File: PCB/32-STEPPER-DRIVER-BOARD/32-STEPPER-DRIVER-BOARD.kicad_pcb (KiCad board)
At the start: 4 copper layers, 100 x 100 mm, 346 parts, among them J1 MEC2-30-01-X-TH1-NP-WT, J2 MEC2-30-01-X-TH1-NP-WT, J3 MEC2-30-01-X-TH1-NP-WT, J4 MEC2-30-01-X-TH1-NP-WT, J5 IPS1-125-01-S-D, J6 UMPT-06-01-X-RA-WT-P-X, U1 74HC595, U10 74HC595, U11 74HC595, U12 74HC595, U13 74HC595, U14 74HC595, U15 74HC595, U17 74HC595, U18 74HC595, U19 74HC595, U2 74HC595, U20 74HC595, U21 74HC595, U22 74HC595, U3 74HC595, U4 74HC595, U5 74HC595, U6 74HC595, U7 74HC595, U9 74HC595

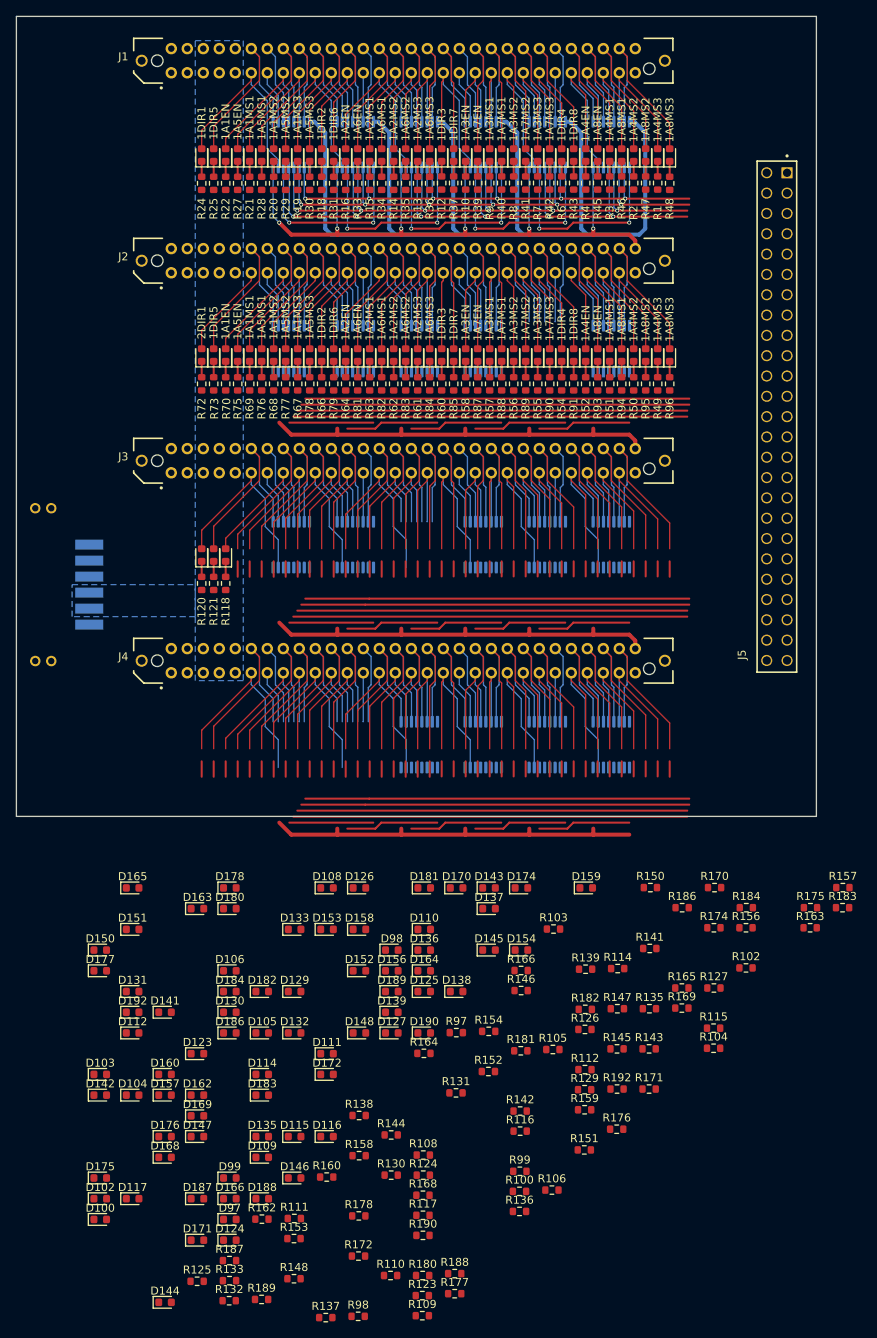
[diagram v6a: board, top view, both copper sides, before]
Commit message: LED's and resistors placed
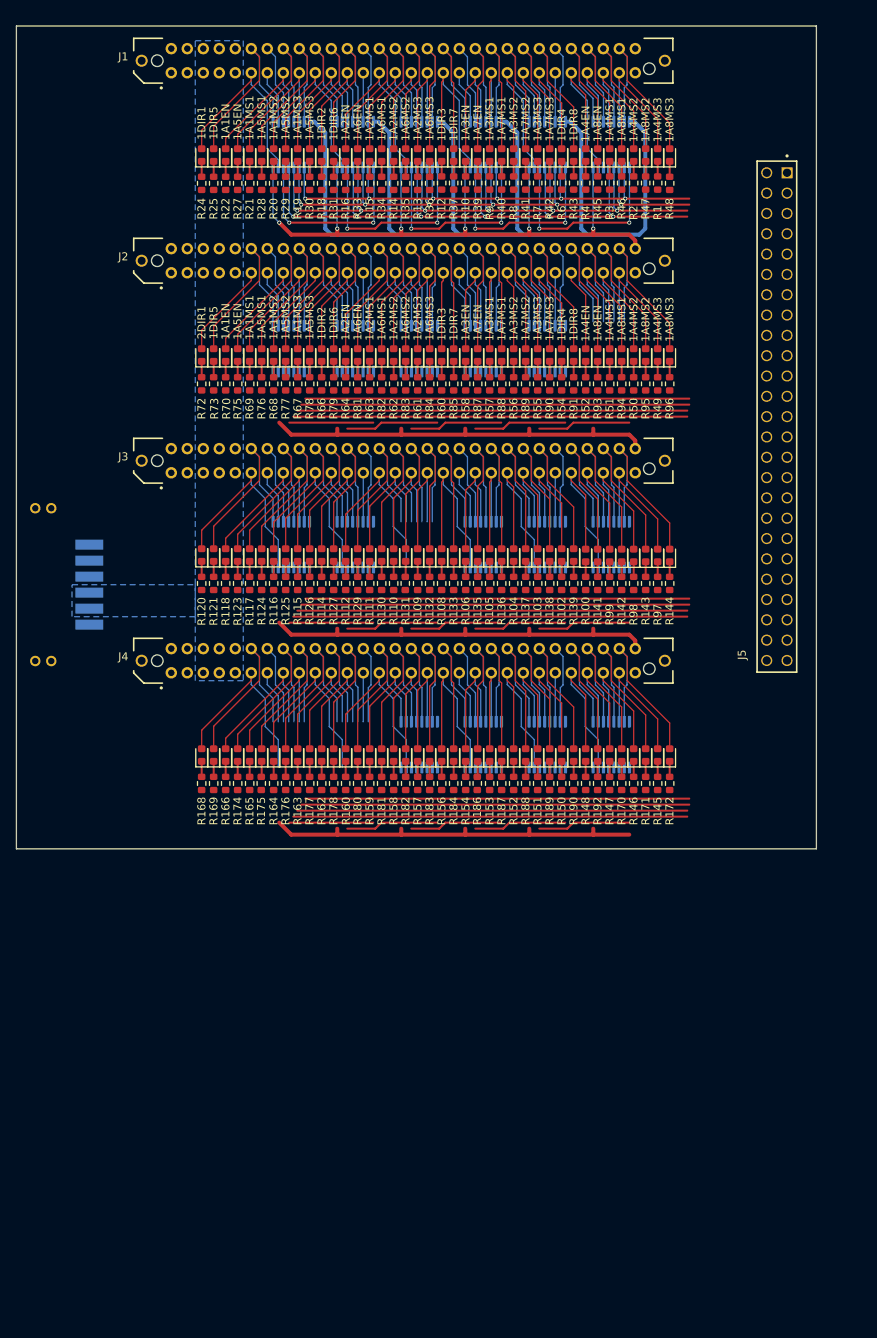
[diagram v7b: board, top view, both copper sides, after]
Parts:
- moved D144 112.7 mm to (122.3, 81.3), turned to 90 degrees
- moved D100 102.8 mm to (111.8, 81.3), turned to 90 degrees
- moved D102 99.0 mm to (108.8, 81.3), turned to 90 degrees
- moved D97 98.7 mm to (120.8, 81.3), turned to 90 degrees
- moved R98 97.9 mm to (117.8, 84.8), turned to -90 degrees
- moved R137 95.1 mm to (104.3, 84.8), turned to -90 degrees
- moved D142 93.8 mm to (116.3, 81.3), turned to 90 degrees
- moved R132 93.1 mm to (92.3, 84.8), turned to -90 degrees
- moved R123 92.0 mm to (68.3, 84.8), turned to -90 degrees
- moved R133 91.5 mm to (95.3, 84.8), turned to -90 degrees
- moved R109 91.5 mm to (90.8, 84.8), turned to -90 degrees
- moved D99 91.2 mm to (114.8, 81.3), turned to 90 degrees
- moved R125 87.9 mm to (74.3, 84.8), turned to -90 degrees
- moved R110 86.5 mm to (87.8, 84.8), turned to -90 degrees
- moved D124 85.7 mm to (71.3, 81.3), turned to 90 degrees
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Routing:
- net 2DIR7: track 24.8 -> 0.00 mm
- net 2A8MS3: track 0.00 -> 24.8 mm
- net 2A8MS2: track 0.00 -> 24.4 mm
- net 2DIR8: track 48.4 -> 24.0 mm
- net 2A8MS1: track 0.00 -> 24.3 mm
- net 2A7MS3: track 48.1 -> 23.9 mm
- net 2A8EN: track 0.00 -> 24.1 mm
- net 2A7MS2: track 47.9 -> 23.7 mm
- net 2A4MS3: track 0.00 -> 17.6 mm
- net 2DIR3: track 27.2 -> 9.58 mm
- net 2DIR4: track 34.5 -> 17.0 mm
- net 2A4MS2: track 0.00 -> 17.5 mm
- net 2A4MS1: track 0.00 -> 17.3 mm
- net 2A3MS3: track 34.3 -> 16.9 mm
- net Net-(D48-Pad1): track 5.77 -> 1.93 mm
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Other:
- board size 100 x 100 mm -> 100 x 102.8 mm

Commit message: re-routing bottom layer
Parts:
- moved U17 43.9 mm to (109.8, 106.7)
- moved U12 43.7 mm to (110.1, 81.4)
- moved U6 43.2 mm to (110.1, 55.1)
- moved U13 12.8 mm to (102.3, 81.4)
- moved U18 12.7 mm to (102.4, 106.5)
- moved U19 12.7 mm to (94.4, 106.5)
- moved U20 12.7 mm to (86.4, 106.5)
- moved U21 12.7 mm to (78.4, 106.5)
- moved U14 12.6 mm to (94.5, 81.7)
- moved U15 12.1 mm to (87.0, 81.5)
- moved U16 4.95 mm to (78.4, 81.8)
- moved U10 4.94 mm to (86.1, 55.1)
- moved U11 4.94 mm to (78.1, 55.1)
- moved U7 4.94 mm to (102.1, 55.1)
- moved U9 4.94 mm to (94.1, 55.1)
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- renumbered U17 to U16, U18 to U17, U19 to U18, U20 to U19, U21 to U20, U22 to U21
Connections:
- U10 pad 1: 2A6MS2 -> 2A5MS3
- U10 pad 15: 2A2MS2 -> 2A1MS3
- U10 pad 2: 2A2MS3 -> 2DIR2
- U10 pad 3: 2A6MS3 -> 2DIR6
- U10 pad 4: 2A1MS2 -> 2A2EN
- U10 pad 5: 2A5MS2 -> 2A6EN
- U10 pad 6: 2A1MS3 -> 2A2MS1
- U10 pad 7: 2A5MS3 -> 2A6MS1
- U11 pad 1: 2DIR6 -> 2DIR5
- U11 pad 15: 2DIR2 -> 2DIR1
- U11 pad 2: 2DIR1 -> 2A1EN
- U11 pad 3: 2DIR5 -> 2A5EN
- U11 pad 4: 2A1EN -> 2A1MS1
- U11 pad 5: 2A5EN -> 2A5MS1
- U11 pad 6: 2A1MS1 -> 2A1MS2
- U11 pad 7: 2A5MS1 -> 2A5MS2
- U12 pad 4: 2A1EN -> 3A4MS2
- U15 pad 1: 3DIR6 -> 3A6MS3
- U15 pad 15: 3DIR2 -> 3A2MS3
- U16 pad 1: 3A6EN -> 3DIR6
- U16 pad 15: 3A2EN -> 3DIR2
- U16 pad 2: 3A2MS1 -> 3A2EN
- U16 pad 3: 3A6MS1 -> 3A6EN
- U16 pad 4: 3A2MS2 -> 3A2MS1
- U16 pad 5: 3A6MS2 -> 3A6MS1
- U16 pad 6: 3A2MS3 -> 3A2MS2
- U16 pad 7: 3A6MS3 -> 3A6MS2
- U2 pad 1: 1A7MS2 -> 1A7MS1
- U2 pad 15: 1A3MS2 -> 1A3MS1
- U2 pad 2: 1A3MS3 -> 1A3MS2
- U2 pad 3: 1A7MS3 -> 1A7MS2
- U2 pad 4: 1DIR4 -> 1A3MS3
- U2 pad 5: 1DIR8 -> 1A7MS3
- U2 pad 6: 1DIR3 -> 1DIR4
- U2 pad 7: 1DIR7 -> 1DIR8
- U3 pad 1: 1A7EN -> 1A6MS2
- U3 pad 15: 1A3EN -> 1A2MS2
- U3 pad 2: 1A3MS1 -> 1A2MS3
- U3 pad 3: 1A7MS1 -> 1A6MS3
- U3 pad 4: 1A2EN -> 1DIR3
- U3 pad 5: 1A6EN -> 1DIR7
- U3 pad 6: 1A2MS1 -> 1A3EN
- U3 pad 7: 1A6MS1 -> 1A7EN
- U4 pad 1: 1A6MS2 -> 1A5MS3
- U4 pad 15: 1A2MS2 -> 1A1MS3
- U4 pad 2: 1A2MS3 -> 1DIR2
- U4 pad 3: 1A6MS3 -> 1DIR6
- U4 pad 4: 1A1MS2 -> 1A2EN
- U4 pad 5: 1A5MS2 -> 1A6EN
- U4 pad 6: 1A1MS3 -> 1A2MS1
- U4 pad 7: 1A5MS3 -> 1A6MS1
- U5 pad 1: 1DIR6 -> 1DIR5
- U5 pad 15: 1DIR2 -> 1DIR1
- U5 pad 2: 1DIR1 -> 1A1EN
- U5 pad 3: 1DIR5 -> 1A5EN
- U5 pad 4: 1A1EN -> 1A1MS1
- U5 pad 5: 1A5EN -> 1A5MS1
- U5 pad 6: 1A1MS1 -> 1A1MS2
- U5 pad 7: 1A5MS1 -> 1A5MS2
- U7 pad 1: 2A7MS2 -> 2A7MS1
- U7 pad 15: 2A3MS2 -> 2A3MS1
- U7 pad 2: 2A3MS3 -> 2A3MS2
- U7 pad 3: 2A7MS3 -> 2A7MS2
- U7 pad 4: 2DIR4 -> 2A3MS3
- U7 pad 5: 2DIR8 -> 2A7MS3
- U7 pad 6: 2DIR3 -> 2DIR4
- U7 pad 7: 2DIR7 -> 2DIR8
- U9 pad 1: 2A7EN -> 2A6MS2
- U9 pad 15: 2A3EN -> 2A2MS2
- U9 pad 2: 2A3MS1 -> 2A2MS3
- U9 pad 3: 2A7MS1 -> 2A6MS3
- U9 pad 4: 2A2EN -> 2DIR3
- U9 pad 5: 2A6EN -> 2DIR7
- U9 pad 6: 2A2MS1 -> 2A3EN
- U9 pad 7: 2A6MS1 -> 2A7EN
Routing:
- net GND: track 132.1 -> 0.00 mm
- net +5V: track 244.1 -> 198.7 mm, vias 6 -> 0
- net ~{OE}: track 235.3 -> 197.0 mm, vias 6 -> 0
- net RCLK: track 228.4 -> 195.0 mm, vias 6 -> 0
- net 3A2EN: track 49.4 -> 17.4 mm
- net SRCLK: track 222.5 -> 194.0 mm, vias 6 -> 0
- net 3A6EN: track 49.9 -> 24.2 mm
- net 3A8MS1: track 0.00 -> 25.5 mm
- net 2A5MS1: track 0.00 -> 25.4 mm
- net 4DIR7: track 48.1 -> 22.8 mm
- net 2A5MS3: track 0.00 -> 25.2 mm
- net 2A1MS3: track 0.00 -> 24.9 mm
- net 2A5MS2: track 0.00 -> 24.7 mm
- net 4DIR3: track 40.4 -> 15.8 mm
- net 3A6MS1: track 48.5 -> 24.1 mm
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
